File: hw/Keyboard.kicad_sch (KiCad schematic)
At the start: 19 parts, among them J1000 USB-61400416121, J1001 FC68125, J1002 FC68125, J1003 FC68125, J2000 FC68125, J3000 FC68125, J4000 FC68125, X1 Audio_Cable_3.5mm_4Pin, X2 Audio_Cable_3.5mm_4Pin, X3 Audio_Cable_3.5mm_4Pin

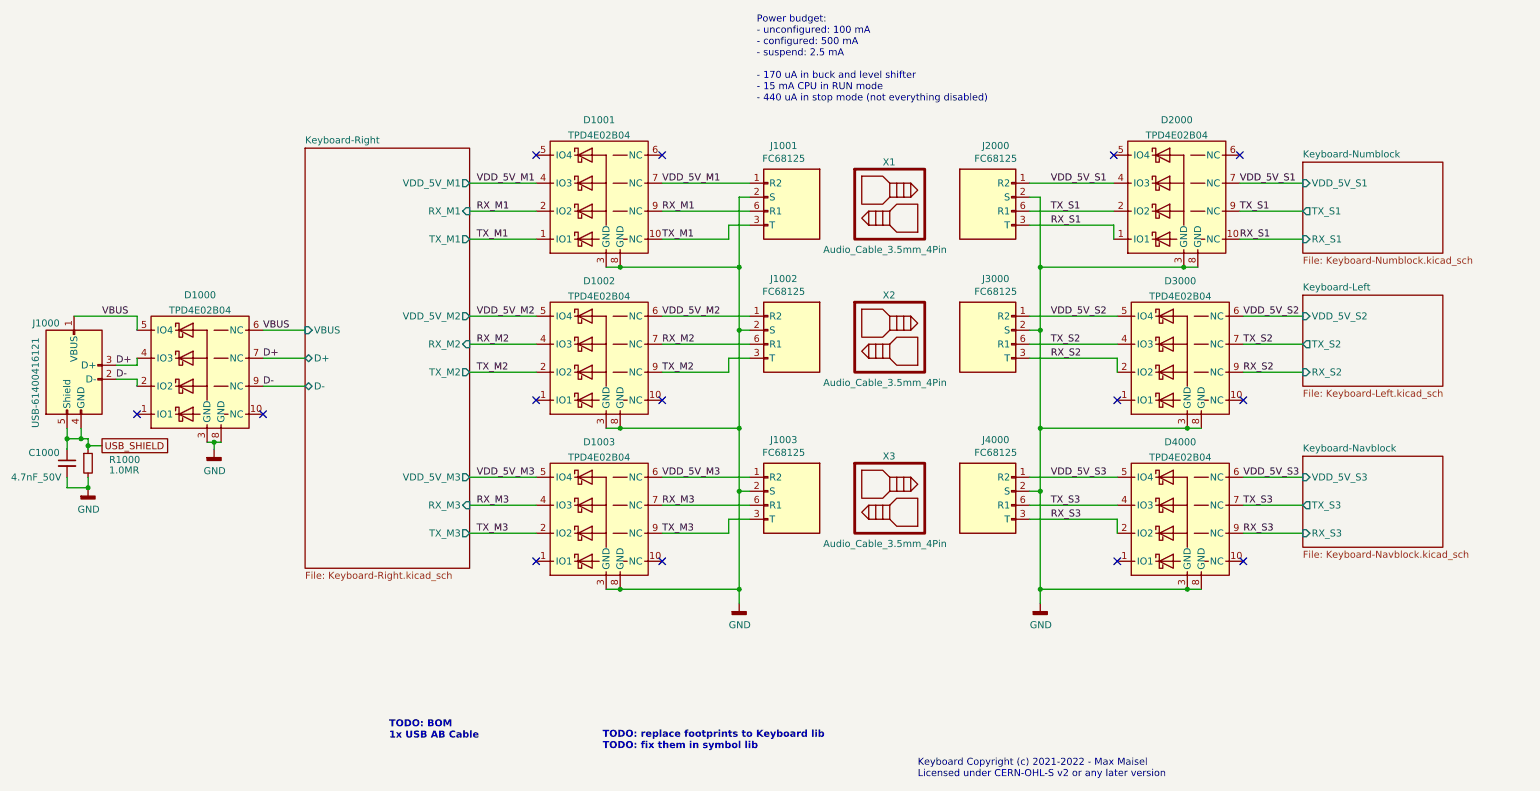
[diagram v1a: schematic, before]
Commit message: Update schematic:
- Add ESD protection.
- Adjust distance bolts so they fit to the MX mounting plate.
- Make key layout symmetric.
- Add resistor to TX driver outputs.
- Use alternate IO functions on inter-board connectors.
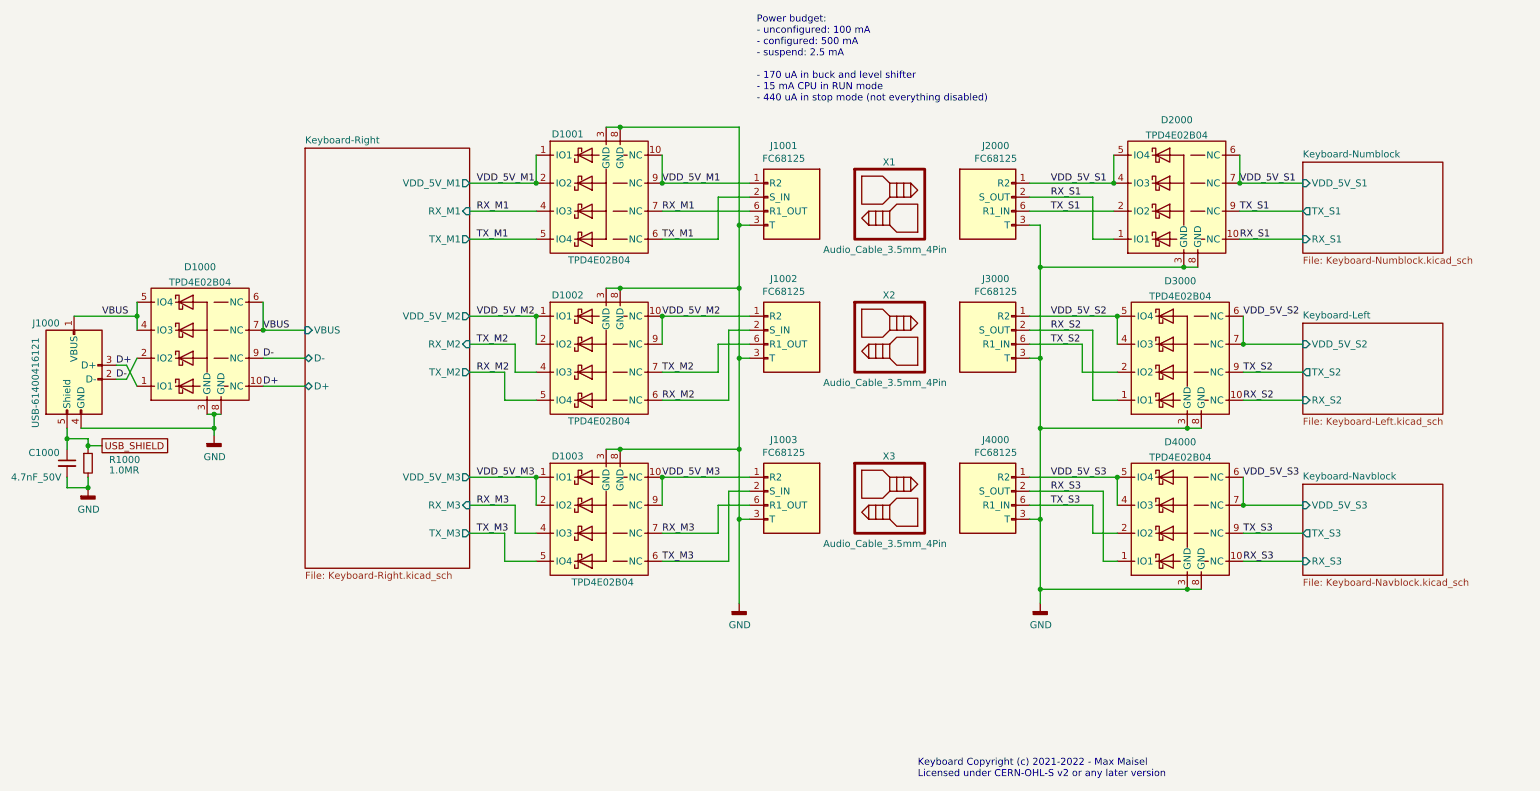
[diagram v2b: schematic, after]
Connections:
- net D+: now also D1000.1 (IO1), D1000.10 (NC); no longer D1000.4 (IO3), D1000.7 (NC)
- net GND: now also J1000.4 (GND), J1001.3 (T), J1002.3 (T), J1003.3 (T), J2000.3 (T), J3000.3 (T), J4000.3 (T); no longer J1001.2 (S), J1002.2 (S), J1003.2 (S), J2000.2 (S), J3000.2 (S), J4000.2 (S)
- net RX_M1: now also D1001.4 (IO3), D1001.7 (NC); no longer D1001.2 (IO2), D1001.9 (NC)
- net RX_M2: now also D1002.5 (IO4), D1002.6 (NC), J1002.2 (S); no longer D1002.4 (IO3), D1002.7 (NC), J1002.6 (R1)
- net RX_S1: now also J2000.2 (S); no longer J2000.3 (T)
- net RX_S2: now also D3000.1 (IO1), D3000.10 (NC), J3000.2 (S); no longer D3000.2 (IO2), D3000.9 (NC), J3000.3 (T)
- net RX_S3: now also D4000.1 (IO1), D4000.10 (NC), J4000.2 (S); no longer D4000.2 (IO2), D4000.9 (NC), J4000.3 (T)
- net TX_M1: now also D1001.5 (IO4), D1001.6 (NC), J1001.2 (S); no longer D1001.1 (IO1), D1001.10 (NC), J1001.3 (T)
- net TX_M2: now also D1002.4 (IO3), D1002.7 (NC), J1002.6 (R1); no longer D1002.2 (IO2), D1002.9 (NC), J1002.3 (T)
- net TX_M3: now also D1003.5 (IO4), D1003.6 (NC), J1003.2 (S); no longer D1003.2 (IO2), D1003.9 (NC), J1003.3 (T)
- net TX_S2: now also D3000.2 (IO2), D3000.9 (NC); no longer D3000.4 (IO3), D3000.7 (NC)
- net TX_S3: now also D4000.2 (IO2), D4000.9 (NC); no longer D4000.4 (IO3), D4000.7 (NC)
- net USB_SHIELD: no longer J1000.4 (GND)
- net VBUS: now also D1000.4 (IO3), D1000.7 (NC)
- net VDD_5V_M1: now also D1001.1 (IO1), D1001.10 (NC), D1001.2 (IO2), D1001.9 (NC); no longer D1001.4 (IO3), D1001.7 (NC)
- net VDD_5V_M2: now also D1002.1 (IO1), D1002.10 (NC), D1002.2 (IO2), D1002.9 (NC); no longer D1002.5 (IO4), D1002.6 (NC)
- net VDD_5V_M3: now also D1003.1 (IO1), D1003.10 (NC), D1003.2 (IO2), D1003.9 (NC); no longer D1003.5 (IO4), D1003.6 (NC)
- net VDD_5V_S1: now also D2000.5 (IO4), D2000.6 (NC)
- net VDD_5V_S2: now also D3000.4 (IO3), D3000.7 (NC)
- net VDD_5V_S3: now also D4000.4 (IO3), D4000.7 (NC)
- no-connect marks 14 -> 0
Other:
- note removed: "TODO: BOM 1x USB AB Cable"
- note removed: "TODO: replace footprints to Keyboard lib TODO: fix them in symbol lib"
- moved on the sheet: D1000, D1001, D1002, D1003
